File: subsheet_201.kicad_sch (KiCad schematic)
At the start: 7 parts, among them J202 BRS — To IKBD, U201 MC6850_PHY

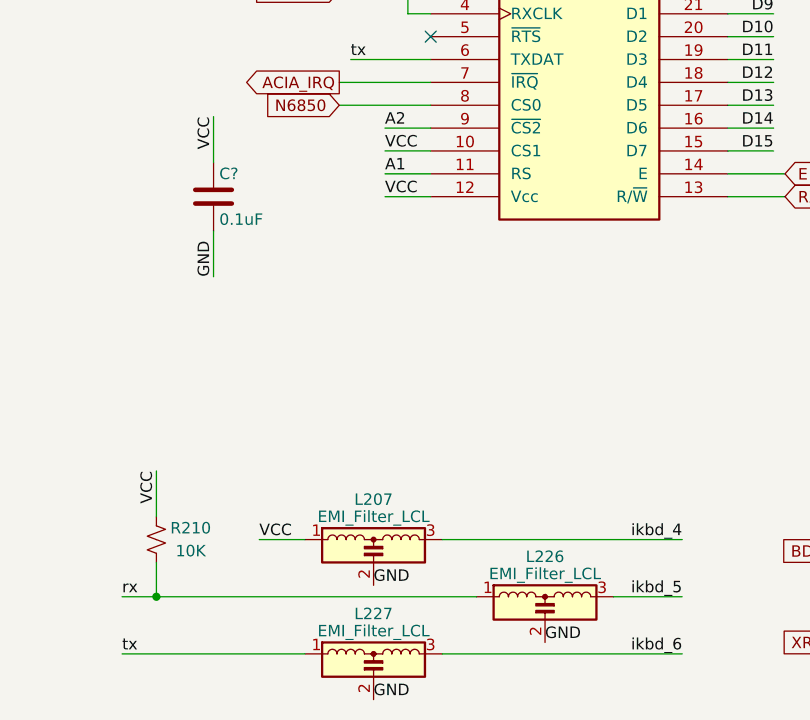
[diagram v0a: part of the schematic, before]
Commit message: Resolves #3 : [schematic] annotate video port with signal name
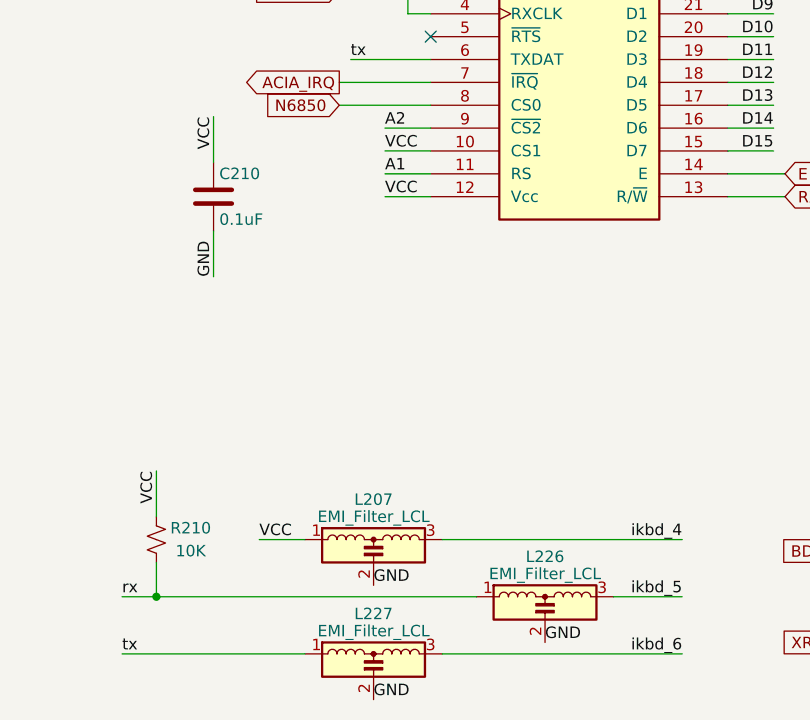
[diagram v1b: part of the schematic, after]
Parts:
- gave numbers to parts that had none: 1
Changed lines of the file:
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@@
     (stroke (width 0) (type default))
   )
-  (label "VCC" (at 69.85 114.3 0)
-    (effects (font (size 1.27 1.27)) (justify left bottom))
-  )
-  (label "ikbd_4" (at 116.84 114.3 180)
-    (effects (font (size 1.27 1.27)) (justify right bottom))
-  )
-  (label "GND" (at 140.97 110.49 0)
-    (effects (font (size 1.27 1.27)) (justify left bottom))
-  )
-  (label "GND" (at 140.97 128.27 0)
-    (effects (font (size 1.27 1.27)) (justify left bottom))
-  )
-  (label "D14" (at 127 68.58 180)
-    (effects (font (size 1.27 1.27)) (justify right bottom))
-  )
-  (label "ikbd_6" (at 138.43 123.19 0)
-    (effects (font (size 1.27 1.27)) (justify left bottom))
-  )
-  (label "VCC" (at 83.82 76.2 0)
-    (effects (font (size 1.27 1.27)) (justify left bottom))
-  )
-  (label "D10" (at 127 58.42 180)
-    (effects (font (size 1.27 1.27)) (justify right bottom))
-  )
-  (label "A2" (at 83.82 68.58 0)
-    (effects (font (size 1.27 1.27)) (justify left bottom))
-  )
-  (label "A1" (at 83.82 73.66 0)
-    (effects (font (size 1.27 1.27)) (justify left bottom))
-  )
-  (label "GND" (at 64.77 85.09 90)
-    (effects (font (size 1.27 1.27)) (justify left bottom))
-  )
-  (label "D11" (at 127 60.96 180)
-    (effects (font (size 1.27 1.27)) (justify right bottom))
-  )
-  (label "D9" (at 127 55.88 180)
-    (effects (font (size 1.27 1.27)) (justify right bottom))
-  )
-  (label "ikbd_5" (at 138.43 120.65 0)
-    (effects (font (size 1.27 1.27)) (justify left bottom))
-  )
-  (label "rx" (at 80.01 50.8 0)
-    (effects (font (size 1.27 1.27)) (justify left bottom))
-  )
-  (label "VCC" (at 83.82 71.12 0)
-    (effects (font (size 1.27 1.27)) (justify left bottom))
-  )
-  (label "tx" (at 54.61 127 0)
-    (effects (font (size 1.27 1.27)) (justify left bottom))
-  )
-  (label "GND" (at 82.55 119.38 0)
-    (effects (font (size 1.27 1.27)) (justify left bottom))
-  )
-  (label "GND" (at 82.55 132.08 0)
-    (effects (font (size 1.27 1.27)) (justify left bottom))
-  )
-  (label "ikbd_4" (at 138.43 118.11 0)
-    (effects (font (size 1.27 1.27)) (justify left bottom))
-  )
-  (label "A[1..23]" (at 44.45 25.4 0)
-    (effects (font (size 1.27 1.27)) (justify left bottom))
-  )
-  (label "ikbd_6" (at 116.84 127 180)
-    (effects (font (size 1.27 1.27)) (justify right bottom))
-  )
-  (label "VCC" (at 64.77 67.31 270)
-    (effects (font (size 1.27 1.27)) (justify right bottom))
-  )
-  (label "GND" (at 83.82 48.26 0)
-    (effects (font (size 1.27 1.27)) (justify left bottom))
-  )
-  (label "D13" (at 127 66.04 180)
-    (effects (font (size 1.27 1.27)) (justify right bottom))
-  )
-  (label "D15" (at 127 71.12 180)
-    (effects (font (size 1.27 1.27)) (justify right bottom))
-  )
-  (label "VCC" (at 58.42 106.68 270)
-    (effects (font (size 1.27 1.27)) (justify right bottom))
-  )
-  (label "GND" (at 127 48.26 180)
-    (effects (font (size 1.27 1.27)) (justify right bottom))
-  )
-  (label "D8" (at 127 53.34 180)
-    (effects (font (size 1.27 1.27)) (justify right bottom))
-  )
-  (label "tx" (at 80.01 60.96 0)
-    (effects (font (size 1.27 1.27)) (justify left bottom))
-  )
-  (label "rx" (at 54.61 120.65 0)
-    (effects (font (size 1.27 1.27)) (justify left bottom))
-  )
-  (label "D[0..15]" (at 165.1 25.4 180)
-    (effects (font (size 1.27 1.27)) (justify right bottom))
-  )
-  (label "ikbd_5" (at 116.84 120.65 180)
-    (effects (font (size 1.27 1.27)) (justify right bottom))
-  )
-  (label "GND" (at 101.6 125.73 0)
-    (effects (font (size 1.27 1.27)) (justify left bottom))
-  )
-  (label "D12" (at 127 63.5 180)
+  (label "VCC" (at 69.85 114.3 0) (fields_autoplaced)
+    (effects (font (size 1.27 1.27)) (justify left bottom))
+  )
+  (label "ikbd_4" (at 116.84 114.3 180) (fields_autoplaced)
+    (effects (font (size 1.27 1.27)) (justify right bottom))
+  )
+  (label "GND" (at 140.97 110.49 0) (fields_autoplaced)
+    (effects (font (size 1.27 1.27)) (justify left bottom))
+  )
+  (label "GND" (at 140.97 128.27 0) (fields_autoplaced)
+    (effects (font (size 1.27 1.27)) (justify left bottom))
+  )
+  (label "D14" (at 127 68.58 180) (fields_autoplaced)
+    (effects (font (size 1.27 1.27)) (justify right bottom))
+  )
+  (label "ikbd_6" (at 138.43 123.19 0) (fields_autoplaced)
+    (effects (font (size 1.27 1.27)) (justify left bottom))
+  )
+  (label "VCC" (at 83.82 76.2 0) (fields_autoplaced)
+    (effects (font (size 1.27 1.27)) (justify left bottom))
+  )
+  (label "D10" (at 127 58.42 180) (fields_autoplaced)
+    (effects (font (size 1.27 1.27)) (justify right bottom))
+  )
+  (label "A2" (at 83.82 68.58 0) (fields_autoplaced)
+    (effects (font (size 1.27 1.27)) (justify left bottom))
+  )
+  (label "A1" (at 83.82 73.66 0) (fields_autoplaced)
+    (effects (font (size 1.27 1.27)) (justify left bottom))
+  )
+  (label "GND" (at 64.77 85.09 90) (fields_autoplaced)
+    (effects (font (size 1.27 1.27)) (justify left bottom))
+  )
+  (label "D11" (at 127 60.96 180) (fields_autoplaced)
+    (effects (font (size 1.27 1.27)) (justify right bottom))
+  )
+  (label "D9" (at 127 55.88 180) (fields_autoplaced)
+    (effects (font (size 1.27 1.27)) (justify right bottom))
+  )
+  (label "ikbd_5" (at 138.43 120.65 0) (fields_autoplaced)
+    (effects (font (size 1.27 1.27)) (justify left bottom))
+  )
+  (label "rx" (at 80.01 50.8 0) (fields_autoplaced)
+    (effects (font (size 1.27 1.27)) (justify left bottom))
+  )
+  (label "VCC" (at 83.82 71.12 0) (fields_autoplaced)
+    (effects (font (size 1.27 1.27)) (justify left bottom))
+  )
+  (label "tx" (at 54.61 127 0) (fields_autoplaced)
+    (effects (font (size 1.27 1.27)) (justify left bottom))
+  )
+  (label "GND" (at 82.55 119.38 0) (fields_autoplaced)
+    (effects (font (size 1.27 1.27)) (justify left bottom))
+  )
+  (label "GND" (at 82.55 132.08 0) (fields_autoplaced)
+    (effects (font (size 1.27 1.27)) (justify left bottom))
+  )
+  (label "ikbd_4" (at 138.43 118.11 0) (fields_autoplaced)
+    (effects (font (size 1.27 1.27)) (justify left bottom))
+  )
+  (label "A[1..23]" (at 44.45 25.4 0) (fields_autoplaced)
+    (effects (font (size 1.27 1.27)) (justify left bottom))
+  )
+  (label "ikbd_6" (at 116.84 127 180) (fields_autoplaced)
+    (effects (font (size 1.27 1.27)) (justify right bottom))
+  )
+  (label "VCC" (at 64.77 67.31 270) (fields_autoplaced)
+    (effects (font (size 1.27 1.27)) (justify right bottom))
+  )
+  (label "GND" (at 83.82 48.26 0) (fields_autoplaced)
+    (effects (font (size 1.27 1.27)) (justify left bottom))
+  )
+  (label "D13" (at 127 66.04 180) (fields_autoplaced)
+    (effects (font (size 1.27 1.27)) (justify right bottom))
+  )
+  (label "D15" (at 127 71.12 180) (fields_autoplaced)
+    (effects (font (size 1.27 1.27)) (justify right bottom))
+  )
+  (label "VCC" (at 58.42 106.68 270) (fields_autoplaced)
+    (effects (font (size 1.27 1.27)) (justify right bottom))
+  )
+  (label "GND" (at 127 48.26 180) (fields_autoplaced)
+    (effects (font (size 1.27 1.27)) (justify right bottom))
+  )
+  (label "D8" (at 127 53.34 180) (fields_autoplaced)
+    (effects (font (size 1.27 1.27)) (justify right bottom))
+  )
+  (label "tx" (at 80.01 60.96 0) (fields_autoplaced)
+    (effects (font (size 1.27 1.27)) (justify left bottom))
+  )
+  (label "rx" (at 54.61 120.65 0) (fields_autoplaced)
+    (effects (font (size 1.27 1.27)) (justify left bottom))
+  )
+  (label "D[0..15]" (at 165.1 25.4 180) (fields_autoplaced)
+    (effects (font (size 1.27 1.27)) (justify right bottom))
+  )
+  (label "ikbd_5" (at 116.84 120.65 180) (fields_autoplaced)
+    (effects (font (size 1.27 1.27)) (justify right bottom))
+  )
+  (label "GND" (at 101.6 125.73 0) (fields_autoplaced)
+    (effects (font (size 1.27 1.27)) (justify left bottom))
+  )
+  (label "D12" (at 127 63.5 180) (fields_autoplaced)
     (effects (font (size 1.27 1.27)) (justify right bottom))
   )
@@
           (reference "U201") (unit 1)
         )
-        (path "/4cb1fb88-82c9-4c30-a4b3-85a871b04fd2/00000000-0000-0000-0000-0000608a2359"
-          (reference "U?") (unit 1)
-        )
       )
     )
@@
           (reference "L207") (unit 1)
         )
-        (path "/4cb1fb88-82c9-4c30-a4b3-85a871b04fd2/00000000-0000-0000-0000-0000608a2359"
-          (reference "L?") (unit 1)
-        )
       )
     )
@@
           (reference "L226") (unit 1)
         )
-        (path "/4cb1fb88-82c9-4c30-a4b3-85a871b04fd2/00000000-0000-0000-0000-0000608a2359"
-          (reference "L?") (unit 1)
-        )
       )
     )
@@
           (reference "L227") (unit 1)
         )
-        (path "/4cb1fb88-82c9-4c30-a4b3-85a871b04fd2/00000000-0000-0000-0000-0000608a2359"
-          (reference "L?") (unit 1)
-        )
       )
     )
@@
   (symbol (lib_id "Device:C") (at 64.77 76.2 0) (unit 1)
     (in_bom yes) (on_board yes) (dnp no)
-    (property "Reference" "C?" (at 65.405 73.66 0)
+    (property "Reference" "C210" (at 65.405 73.66 0)
       (effects (font (size 1.27 1.27)) (justify left))
     )
@@
     (instances
       (project "motherboard"
-        (path "/4cb1fb88-82c9-4c30-a4b3-85a871b04fd2/00000000-0000-0000-0000-0000608a2359"
-          (reference "C?") (unit 1)
-        )
         (path "/4cb1fb88-82c9-4c30-a4b3-85a871b04fd2/00000000-0000-0000-0000-0000608c2344"
           (reference "C210") (unit 1)
-        )
-        (path "/4cb1fb88-82c9-4c30-a4b3-85a871b04fd2/00000000-0000-0000-0000-00006089d0ba"
-          (reference "C?") (unit 1)
         )
       )
@@
           (reference "R210") (unit 1)
         )
-        (path "/4cb1fb88-82c9-4c30-a4b3-85a871b04fd2/00000000-0000-0000-0000-0000608a2359"
-          (reference "R?") (unit 1)
-        )
-      )
+      )
